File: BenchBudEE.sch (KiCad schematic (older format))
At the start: 0 parts

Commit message: Module 2, Unit 14: Defining Your Inputs and Outputs
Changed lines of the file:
@@
 $EndDescr
 $Sheet
-S 1100 5800 1650 1300
+S 2100 2700 1750 3900
 U 52FFA904
 F0 "Arduino" 50
 F1 "Arduino.sch" 50
+F2 "Realy+" O R 3850 5900 60
+F3 "Relay-" I R 3850 6050 60
+F4 "MOSI" O R 3850 5150 60
+F5 "MISO" I R 3850 5300 60
+F6 "SCLK" O R 3850 5450 60
+F7 "CS_N" O R 3850 5600 60
+F8 "LED_EN" O R 3850 4450 60
+F9 "LED_FREQ" O R 3850 4600 60
+F10 "FAN_EN" O R 3850 3900 60
+F11 "TACH_MEAS" I R 3850 4050 60
 $EndSheet
 $Sheet
@@
 F2 "TC_IN+" I R 9500 4400 60
 F3 "TC_IN-" I R 9500 4550 60
+F4 "MOSI" I L 7850 4400 60
+F5 "MISO" O L 7850 4550 60
+F6 "SCLK" I L 7850 4700 60
+F7 "CS_N" I L 7850 4850 60
 $EndSheet
 $Sheet
@@
 F0 "Relay" 50
 F1 "Relay.sch" 50
+F2 "DIN+" I L 7900 5650 60
+F3 "DIN-" O L 7900 5800 60
+F4 "Relay+" I R 9500 5650 60
+F5 "Relay-" O R 9500 5800 60
 $EndSheet
 $Sheet
-S 950  900  1550 1050
+S 2100 1050 1550 1050
 U 52FFAA1F
 F0 "Power" 50
@@
 F0 "LED Driver" 50
 F1 "LED_Driver.sch" 50
+F2 "EN" I L 7900 3050 60
+F3 "FREQ" I L 7900 3200 60
+F4 "String+" O R 9450 3050 60
+F5 "String-" I R 9450 3200 60
 $EndSheet
 $Sheet
@@
 F0 "Fan" 50
 F1 "Fan.sch" 50
+F2 "Power+" O R 9450 1600 60
+F3 "Power-" I R 9450 1750 60
+F4 "Tach" I R 9450 1900 60
+F5 "Tach_out" O L 7800 1900 60
+F6 "Fan_In" I L 7800 1600 60
 $EndSheet
 $Sheet

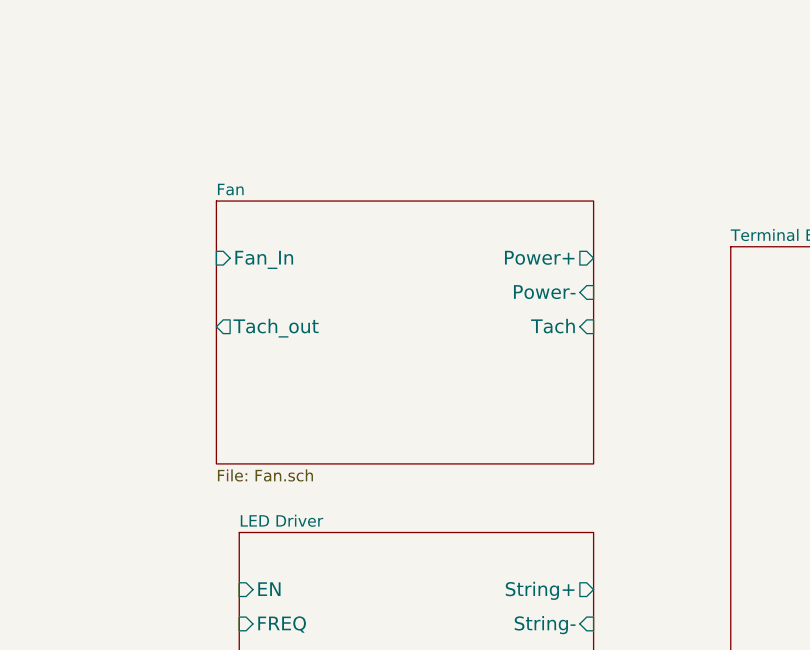
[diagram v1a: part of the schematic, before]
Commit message: Module 3, Unit 4: Understanding The Current/Fan Driver Module
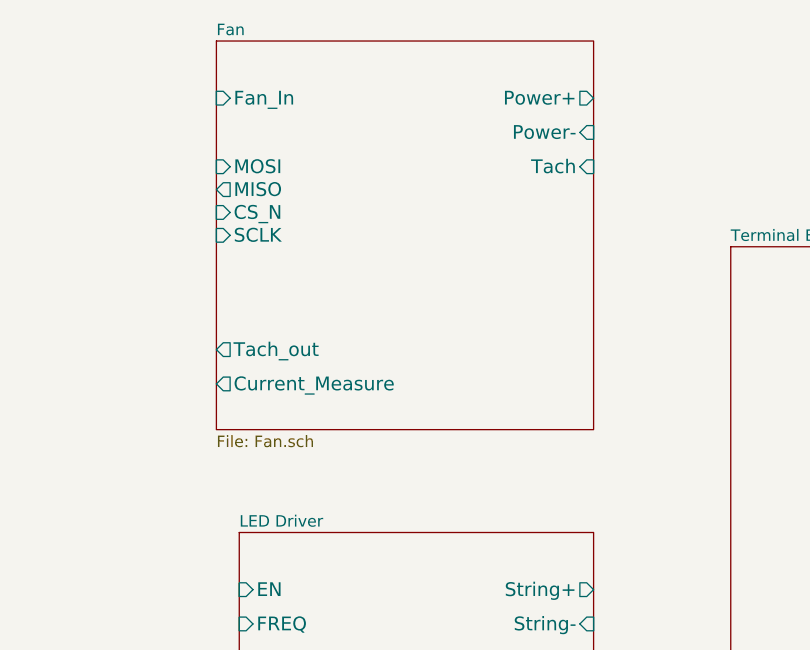
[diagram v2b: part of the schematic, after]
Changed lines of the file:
@@
 $EndSheet
 $Sheet
-S 7800 1350 1650 1150
+S 7800 650  1650 1700
 U 52FFAAD9
 F0 "Fan" 50
 F1 "Fan.sch" 50
-F2 "Power+" O R 9450 1600 60
-F3 "Power-" I R 9450 1750 60
-F4 "Tach" I R 9450 1900 60
-F5 "Tach_out" O L 7800 1900 60
-F6 "Fan_In" I L 7800 1600 60
+F2 "Power+" O R 9450 900 60
+F3 "Power-" I R 9450 1050 60
+F4 "Tach" I R 9450 1200 60
+F5 "Tach_out" O L 7800 2000 60
+F6 "Fan_In" I L 7800 900 60
+F7 "Current_Measure" O L 7800 2150 60
+F8 "MOSI" I L 7800 1200 60
+F9 "MISO" O L 7800 1300 60
+F10 "CS_N" I L 7800 1400 60
+F11 "SCLK" I L 7800 1500 60
 $EndSheet
 $Sheet

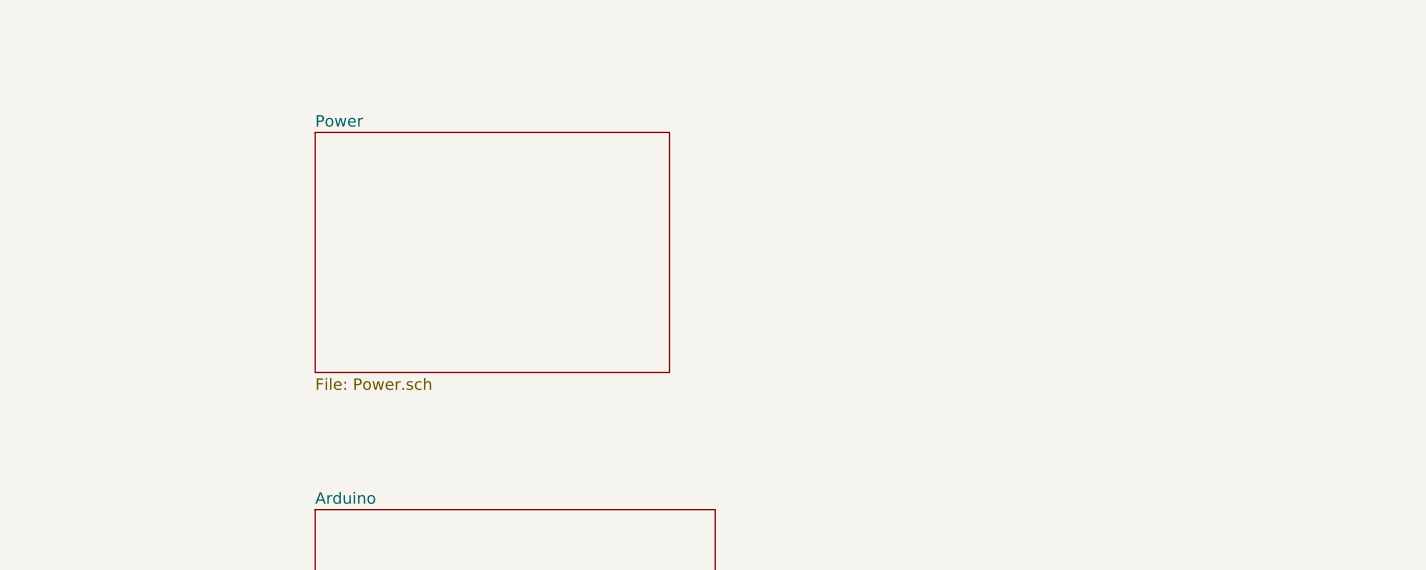
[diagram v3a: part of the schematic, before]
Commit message: Module 3, Unit 6: Understanding The Power Protection And Filtering Module
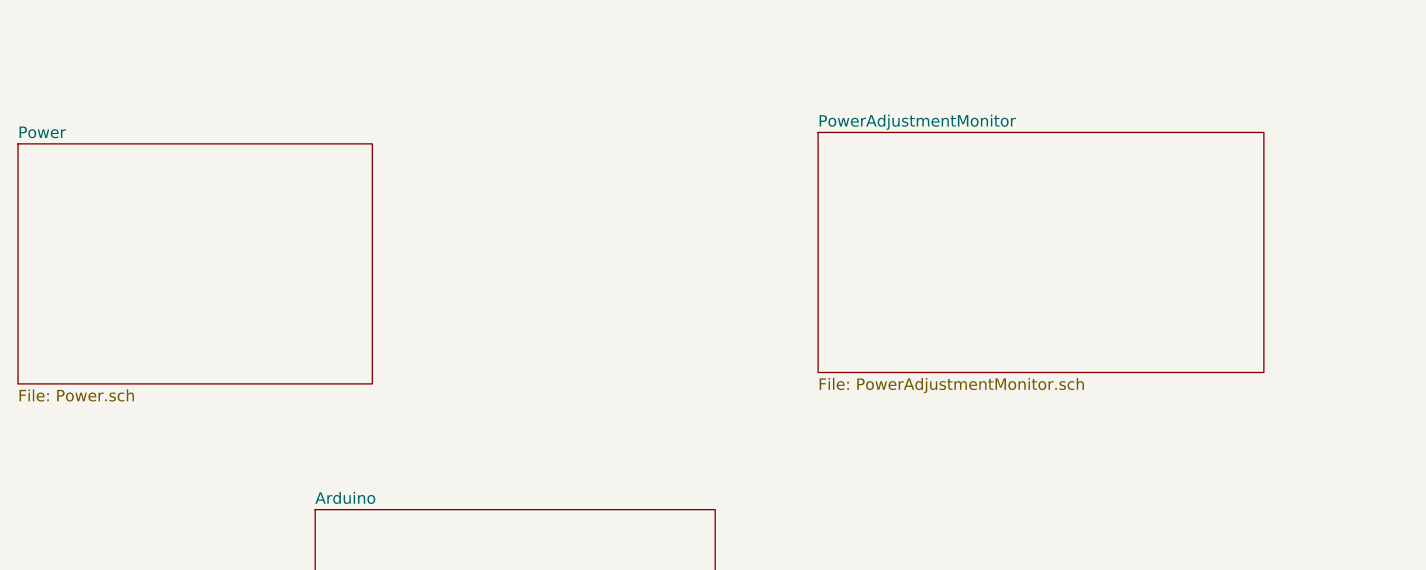
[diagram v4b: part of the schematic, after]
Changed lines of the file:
@@
 $Descr A4 11693 8268
 encoding utf-8
-Sheet 1 8
+Sheet 1 9
 Title ""
 Date ""
@@
 $EndSheet
 $Sheet
-S 2100 1050 1550 1050
+S 800  1100 1550 1050
 U 52FFAA1F
 F0 "Power" 50
@@
 F1 "TerminalBlock.sch" 50
 $EndSheet
+$Sheet
+S 4300 1050 1950 1050
+U 53014FF5
+F0 "PowerAdjustmentMonitor" 50
+F1 "PowerAdjustmentMonitor.sch" 50
+$EndSheet
 $EndSCHEMATC

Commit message: Module 3, Unit 7: Understanding The Power Control, Conditioning And Monitoring Module
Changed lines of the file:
@@
 $EndSheet
 $Sheet
-S 7850 4200 1650 1000
+S 7900 4900 1650 750
 U 52FFA9C4
 F0 "Thermocouple" 50
 F1 "Thermocouple.sch" 50
-F2 "TC_IN+" I R 9500 4400 60
-F3 "TC_IN-" I R 9500 4550 60
-F4 "MOSI" I L 7850 4400 60
-F5 "MISO" O L 7850 4550 60
-F6 "SCLK" I L 7850 4700 60
-F7 "CS_N" I L 7850 4850 60
+F2 "TC_IN+" I R 9550 5100 60
+F3 "TC_IN-" I R 9550 5250 60
+F4 "MOSI" I L 7900 5100 60
+F5 "MISO" O L 7900 5250 60
+F6 "SCLK" I L 7900 5400 60
+F7 "CS_N" I L 7900 5550 60
 $EndSheet
 $Sheet
-S 7900 5450 1600 900
+S 7900 5800 1650 450
 U 52FFA9E6
 F0 "Relay" 50
 F1 "Relay.sch" 50
-F2 "DIN+" I L 7900 5650 60
-F3 "DIN-" O L 7900 5800 60
-F4 "Relay+" I R 9500 5650 60
-F5 "Relay-" O R 9500 5800 60
+F2 "DIN+" I L 7900 5900 60
+F3 "DIN-" O L 7900 6000 60
+F4 "NC" B R 9550 5900 60
+F5 "NO" B R 9550 6000 60
+F6 "COM" B R 9550 6100 60
 $EndSheet
 $Sheet
@@
 $EndSheet
 $Sheet
-S 7900 2800 1550 1050
-U 52FFAA9A
-F0 "LED Driver" 50
-F1 "LED_Driver.sch" 50
-F2 "EN" I L 7900 3050 60
-F3 "FREQ" I L 7900 3200 60
-F4 "String+" O R 9450 3050 60
-F5 "String-" I R 9450 3200 60
-$EndSheet
-$Sheet
-S 7800 650  1650 1700
-U 52FFAAD9
-F0 "Fan" 50
-F1 "Fan.sch" 50
-F2 "Power+" O R 9450 900 60
-F3 "Power-" I R 9450 1050 60
-F4 "Tach" I R 9450 1200 60
-F5 "Tach_out" O L 7800 2000 60
-F6 "Fan_In" I L 7800 900 60
-F7 "Current_Measure" O L 7800 2150 60
-F8 "MOSI" I L 7800 1200 60
-F9 "MISO" O L 7800 1300 60
-F10 "CS_N" I L 7800 1400 60
-F11 "SCLK" I L 7800 1500 60
-$EndSheet
-$Sheet
-S 10050 1550 600  4350
+S 10000 1050 650  5200
 U 52FFAB03
 F0 "Terminal Block" 50
@@
 $EndSheet
 $Sheet
-S 4300 1050 1950 1050
+S 7900 4350 1650 350
+U 52FFAA9A
+F0 "LED Driver" 50
+F1 "LED_Driver.sch" 50
+F2 "EN" I L 7900 4500 60
+F3 "FREQ" I L 7900 4600 60
+F4 "String+" O R 9550 4500 60
+F5 "String-" I R 9550 4600 60
+$EndSheet
+$Sheet
+S 7900 3050 1650 1100
+U 52FFAAD9
+F0 "Fan" 50
+F1 "Fan.sch" 50
+F2 "Power+" O R 9550 3300 60
+F3 "Power-" I R 9550 3450 60
+F4 "Tach" I R 9550 3600 60
+F5 "Tach_out" O L 7900 3900 60
+F6 "Fan_In" I L 7900 3150 60
+F7 "Current_Measure" O L 7900 4000 60
+F8 "MOSI" I L 7900 3400 60
+F9 "MISO" O L 7900 3500 60
+F10 "CS_N" I L 7900 3600 60
+F11 "SCLK" I L 7900 3700 60
+$EndSheet
+$Sheet
+S 5200 1050 1650 1050
 U 53014FF5
 F0 "PowerAdjustmentMonitor" 50
 F1 "PowerAdjustmentMonitor.sch" 50
+F2 "V+_ADJ" O R 6850 1200 60
+F3 "V-_ADJ" O R 6850 1300 60
+F4 "3V3_MON" O L 5200 1250 60
+F5 "5V_MON" O L 5200 1150 60
+F6 "V+_ADJ_MON" O L 5200 1850 60
+F7 "V-_ADJ_MON" O L 5200 1950 60
+F8 "V+_CURR_ADJ_MON" O L 5200 1450 60
+F9 "V-_CURR_ADJ_MON" O L 5200 1550 60
 $EndSheet
 $EndSCHEMATC

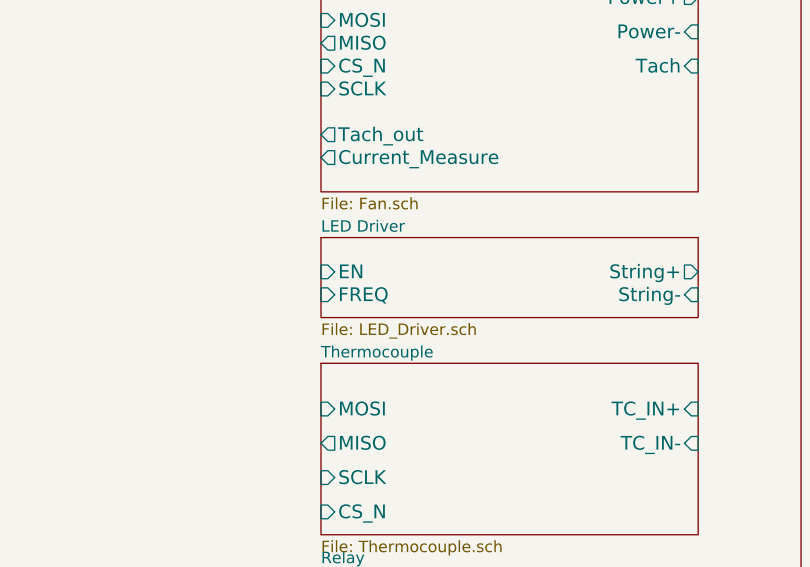
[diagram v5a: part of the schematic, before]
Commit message: Module 3, Unit 8: Understanding The LED Driver Module
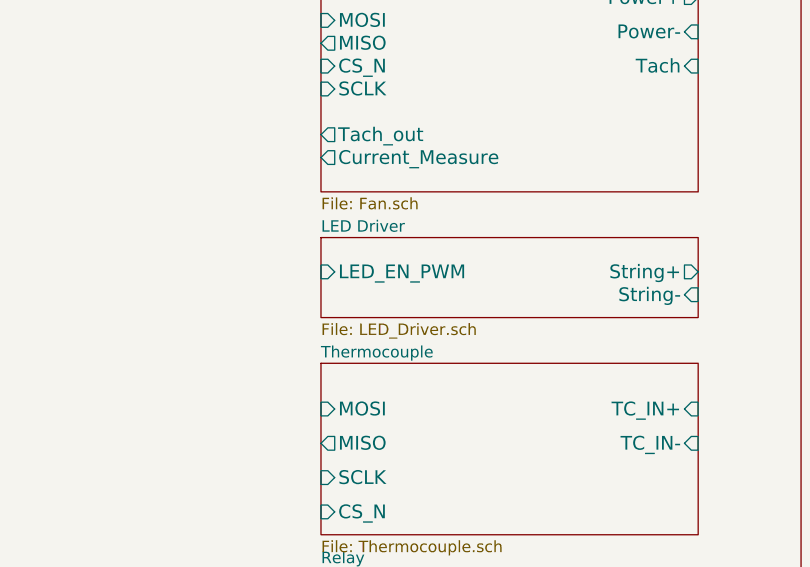
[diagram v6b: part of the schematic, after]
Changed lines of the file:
@@
 F0 "LED Driver" 50
 F1 "LED_Driver.sch" 50
-F2 "EN" I L 7900 4500 60
-F3 "FREQ" I L 7900 4600 60
-F4 "String+" O R 9550 4500 60
-F5 "String-" I R 9550 4600 60
+F2 "String+" O R 9550 4500 60
+F3 "String-" I R 9550 4600 60
+F4 "LED_EN_PWM" I L 7900 4500 60
 $EndSheet
 $Sheet

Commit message: Module 3, Unit 9: Understanding The Arduino Module
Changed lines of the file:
@@
 $EndDescr
 $Sheet
-S 2100 2700 1750 3900
-U 52FFA904
-F0 "Arduino" 50
-F1 "Arduino.sch" 50
-F2 "Realy+" O R 3850 5900 60
-F3 "Relay-" I R 3850 6050 60
-F4 "MOSI" O R 3850 5150 60
-F5 "MISO" I R 3850 5300 60
-F6 "SCLK" O R 3850 5450 60
-F7 "CS_N" O R 3850 5600 60
-F8 "LED_EN" O R 3850 4450 60
-F9 "LED_FREQ" O R 3850 4600 60
-F10 "FAN_EN" O R 3850 3900 60
-F11 "TACH_MEAS" I R 3850 4050 60
-$EndSheet
-$Sheet
-S 7900 4900 1650 750
+S 7900 4350 1650 750
 U 52FFA9C4
 F0 "Thermocouple" 50
 F1 "Thermocouple.sch" 50
-F2 "TC_IN+" I R 9550 5100 60
-F3 "TC_IN-" I R 9550 5250 60
-F4 "MOSI" I L 7900 5100 60
-F5 "MISO" O L 7900 5250 60
-F6 "SCLK" I L 7900 5400 60
-F7 "CS_N" I L 7900 5550 60
+F2 "TC_IN+" I R 9550 4550 60
+F3 "TC_IN-" I R 9550 4700 60
+F4 "MOSI" I L 7900 4550 60
+F5 "MISO" O L 7900 4700 60
+F6 "SCLK" I L 7900 4850 60
+F7 "CS_N" I L 7900 5000 60
 $EndSheet
 $Sheet
@@
 F0 "Relay" 50
 F1 "Relay.sch" 50
-F2 "DIN+" I L 7900 5900 60
-F3 "DIN-" O L 7900 6000 60
-F4 "NC" B R 9550 5900 60
-F5 "NO" B R 9550 6000 60
-F6 "COM" B R 9550 6100 60
+F2 "RELAY_NC" B R 9550 6000 60
+F3 "RELAY_NO" B R 9550 6100 60
+F4 "RELAY_COM" B R 9550 5900 60
+F5 "RELAY+" I L 7900 5900 60
+F6 "RELAY-" O L 7900 6000 60
 $EndSheet
 $Sheet
@@
 $EndSheet
 $Sheet
-S 10000 1050 650  5200
+S 10000 1050 850  5250
 U 52FFAB03
 F0 "Terminal Block" 50
 F1 "TerminalBlock.sch" 50
-$EndSheet
-$Sheet
-S 7900 4350 1650 350
+F2 "V+_ADJ" I L 10000 1200 60
+F3 "V-_ADJ" I L 10000 1300 60
+F4 "FAN_OUT+" O L 10000 3200 60
+F5 "FAN_OUT-" O L 10000 3300 60
+F6 "TACH_IN" I L 10000 3600 60
+F7 "LED_STRING+" O L 10000 5400 60
+F8 "LED_STRING-" O L 10000 5500 60
+F9 "TC_IN+" I L 10000 4550 60
+F10 "TC_IN-" I L 10000 4700 60
+F11 "RELAY_COM" B L 10000 5900 60
+F12 "RELAY_NO" B L 10000 6100 60
+F13 "RELAY_NC" B L 10000 6000 60
+$EndSheet
+$Sheet
+S 7900 5300 1650 350
 U 52FFAA9A
 F0 "LED Driver" 50
 F1 "LED_Driver.sch" 50
-F2 "String+" O R 9550 4500 60
-F3 "String-" I R 9550 4600 60
-F4 "LED_EN_PWM" I L 7900 4500 60
+F2 "LED_EN_PWM" I L 7900 5450 60
+F3 "LED_STRING+" O R 9550 5400 60
+F4 "LED_STRING-" O R 9550 5500 60
 $EndSheet
 $Sheet
@@
 F0 "Fan" 50
 F1 "Fan.sch" 50
-F2 "Power+" O R 9550 3300 60
-F3 "Power-" I R 9550 3450 60
-F4 "Tach" I R 9550 3600 60
-F5 "Tach_out" O L 7900 3900 60
-F6 "Fan_In" I L 7900 3150 60
-F7 "Current_Measure" O L 7900 4000 60
-F8 "MOSI" I L 7900 3400 60
-F9 "MISO" O L 7900 3500 60
-F10 "CS_N" I L 7900 3600 60
-F11 "SCLK" I L 7900 3700 60
+F2 "MOSI" I L 7900 3400 60
+F3 "MISO" O L 7900 3500 60
+F4 "CS_N" I L 7900 3700 60
+F5 "SCLK" I L 7900 3600 60
+F6 "FAN_OUT+" O R 9550 3200 60
+F7 "TACH_IN" I R 9550 3600 60
+F8 "TACH_MEAS" O L 7900 3900 60
+F9 "FAN_EN_N" I L 7900 3200 60
+F10 "CURR_MEAS" O L 7900 4000 60
+F11 "FAN_OUT-" O R 9550 3300 60
 $EndSheet
 $Sheet
@@
 F9 "V-_CURR_ADJ_MON" O L 5200 1550 60
 $EndSheet
+Wire Wire Line
+	6850 1200 10000 1200
+Wire Wire Line
+	6850 1300 10000 1300
+Wire Wire Line
+	9550 3200 10000 3200
+Wire Wire Line
+	9550 3300 10000 3300
+Wire Wire Line
+	9550 3600 10000 3600
+Wire Wire Line
+	9550 5900 10000 5900
+Wire Wire Line
+	9550 6000 10000 6000
+Wire Wire Line
+	9550 6100 10000 6100
+Wire Wire Line
+	3850 3250 4450 3250
+Wire Wire Line
+	4450 3250 4450 1850
+Wire Wire Line
+	4450 1850 5200 1850
+Wire Wire Line
+	5200 1950 4600 1950
+Wire Wire Line
+	4600 1950 4600 3400
+Wire Wire Line
+	4600 3400 3850 3400
+Wire Wire Line
+	3850 3700 5050 3700
+Wire Wire Line
+	5050 3700 5050 3200
+Wire Wire Line
+	5050 3200 7900 3200
+Wire Wire Line
+	3850 3900 5350 3900
+Wire Wire Line
+	5350 3900 5350 3400
+Wire Wire Line
+	5350 3400 7900 3400
+Wire Wire Line
+	3850 4050 5500 4050
+Wire Wire Line
+	5500 4050 5500 3500
+Wire Wire Line
+	5500 3500 7900 3500
+Wire Wire Line
+	3850 4200 5650 4200
+Wire Wire Line
+	5650 4200 5650 3600
+Wire Wire Line
+	5650 3600 7900 3600
+Wire Wire Line
+	3850 4350 5800 4350
+Wire Wire Line
+	5800 4350 5800 3700
+Wire Wire Line
+	5800 3700 7900 3700
+Wire Wire Line
+	9550 4550 10000 4550
+Wire Wire Line
+	10000 4700 9550 4700
+Wire Wire Line
+	9550 5400 10000 5400
+Wire Wire Line
+	9550 5500 10000 5500
+Wire Wire Line
+	7900 3900 6050 3900
+Wire Wire Line
+	6050 3900 6050 4850
+Wire Wire Line
+	6050 4850 3850 4850
+Wire Wire Line
+	7900 4000 6200 4000
+Wire Wire Line
+	6200 4000 6200 5000
+Wire Wire Line
+	6200 5000 3850 5000
+Wire Wire Line
+	7900 4550 7100 4550
+Wire Wire Line
+	7100 4550 7100 3400
+Connection ~ 7100 3400
+Wire Wire Line
+	7900 4700 7000 4700
+Wire Wire Line
+	7000 4700 7000 3500
+Connection ~ 7000 3500
+Wire Wire Line
+	7900 4850 6900 4850
+Wire Wire Line
+	6900 4850 6900 3600
+Connection ~ 6900 3600
+$Sheet
+S 2100 2700 1750 3900
+U 52FFA904
+F0 "Arduino" 50
+F1 "Arduino.sch" 50
+F2 "MOSI" O R 3850 3900 60
+F3 "MISO" I R 3850 4050 60
+F4 "SCLK" O R 3850 4200 60
+F5 "TACH_MEAS" I R 3850 4850 60
+F6 "RELAY+" O R 3850 6050 60
+F7 "RELAY-" I R 3850 6200 60
+F8 "FAN_EN_N" O R 3850 3700 60
+F9 "CURR_MEAS" I R 3850 5000 60
+F10 "V+_ADJ_MON" I R 3850 3250 60
+F11 "V-_ADJ_MON" I R 3850 3400 60
+F12 "LED_EN_PWM" O R 3850 5600 60
+F13 "DAC_CS_N" O R 3850 4350 60
+F14 "ADC_CS_N" O R 3850 5250 60
+$EndSheet
+Wire Wire Line
+	7900 5000 6400 5000
+Wire Wire Line
+	6400 5000 6400 5250
+Wire Wire Line
+	6400 5250 3850 5250
+Wire Wire Line
+	7900 5450 6500 5450
+Wire Wire Line
+	6500 5450 6500 5600
+Wire Wire Line
+	6500 5600 3850 5600
+Wire Wire Line
+	7900 5900 6600 5900
+Wire Wire Line
+	6600 5900 6600 6050
+Wire Wire Line
+	6600 6050 3850 6050
+Wire Wire Line
+	7900 6000 6750 6000
+Wire Wire Line
+	6750 6000 6750 6200
+Wire Wire Line
+	6750 6200 3850 6200
 $EndSCHEMATC
